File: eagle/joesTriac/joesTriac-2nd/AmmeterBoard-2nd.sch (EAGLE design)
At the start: 37 parts, among them IC2 TLC251P, IC3 TLC251_or_311, IC4 INA118P, IC5 TLC251_or_311, IC6 TLC251P, IC7 ACS758ECB-200B-PFF-T, T1 2N3441, X1 1, X2 2, X6 1751264

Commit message: reg save, working on exti
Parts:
- added X3: 1751264, con-phoenix-350:1751264
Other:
- note added: ". +9"
- note added: ". -9"
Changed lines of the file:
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@@
 <part name="SUPPLY31" library="supply2" deviceset="GND" device=""/>
 <part name="SUPPLY32" library="supply2" deviceset="GND" device=""/>
+<part name="X3" library="con-phoenix-350" deviceset="1751264" device=""/>
 </parts>
 <sheets>
@@
 <text x="139.7" y="58.42" size="1.778" layer="91">eventually aplifier can be ommitted</text>
 <text x="91.44" y="-7.62" size="1.778" layer="91">0V .. 3.3V tobe tested</text>
+<text x="35.56" y="48.26" size="1.778" layer="91">.   -9</text>
+<text x="35.56" y="53.34" size="1.778" layer="91">.   +9</text>
 </plain>
 <instances>
@@
 <instance part="SUPPLY31" gate="GND" x="20.32" y="-12.7"/>
 <instance part="SUPPLY32" gate="GND" x="83.82" y="-20.32"/>
+<instance part="X3" gate="-2" x="22.86" y="53.34"/>
+<instance part="X3" gate="-3" x="22.86" y="48.26"/>
 </instances>
 <busses>
@@
 <pinref part="IC2" gate="A" pin="+IN"/>
 <wire x1="-35.56" y1="2.54" x2="-25.4" y2="2.54" width="0.1524" layer="91"/>
-<wire x1="25.4" y1="76.2" x2="38.1" y2="76.2" width="0.1524" layer="91"/>
-<wire x1="38.1" y1="76.2" x2="38.1" y2="22.86" width="0.1524" layer="91"/>
-<wire x1="38.1" y1="22.86" x2="-35.56" y2="22.86" width="0.1524" layer="91"/>
+<wire x1="43.18" y1="22.86" x2="-35.56" y2="22.86" width="0.1524" layer="91"/>
 <wire x1="-35.56" y1="22.86" x2="-35.56" y2="2.54" width="0.1524" layer="91"/>
-</segment>
-</net>
+<wire x1="43.18" y1="76.2" x2="43.18" y2="22.86" width="0.1524" layer="91"/>
+<wire x1="25.4" y1="76.2" x2="43.18" y2="76.2" width="0.1524" layer="91"/>
+</segment>
+</net>

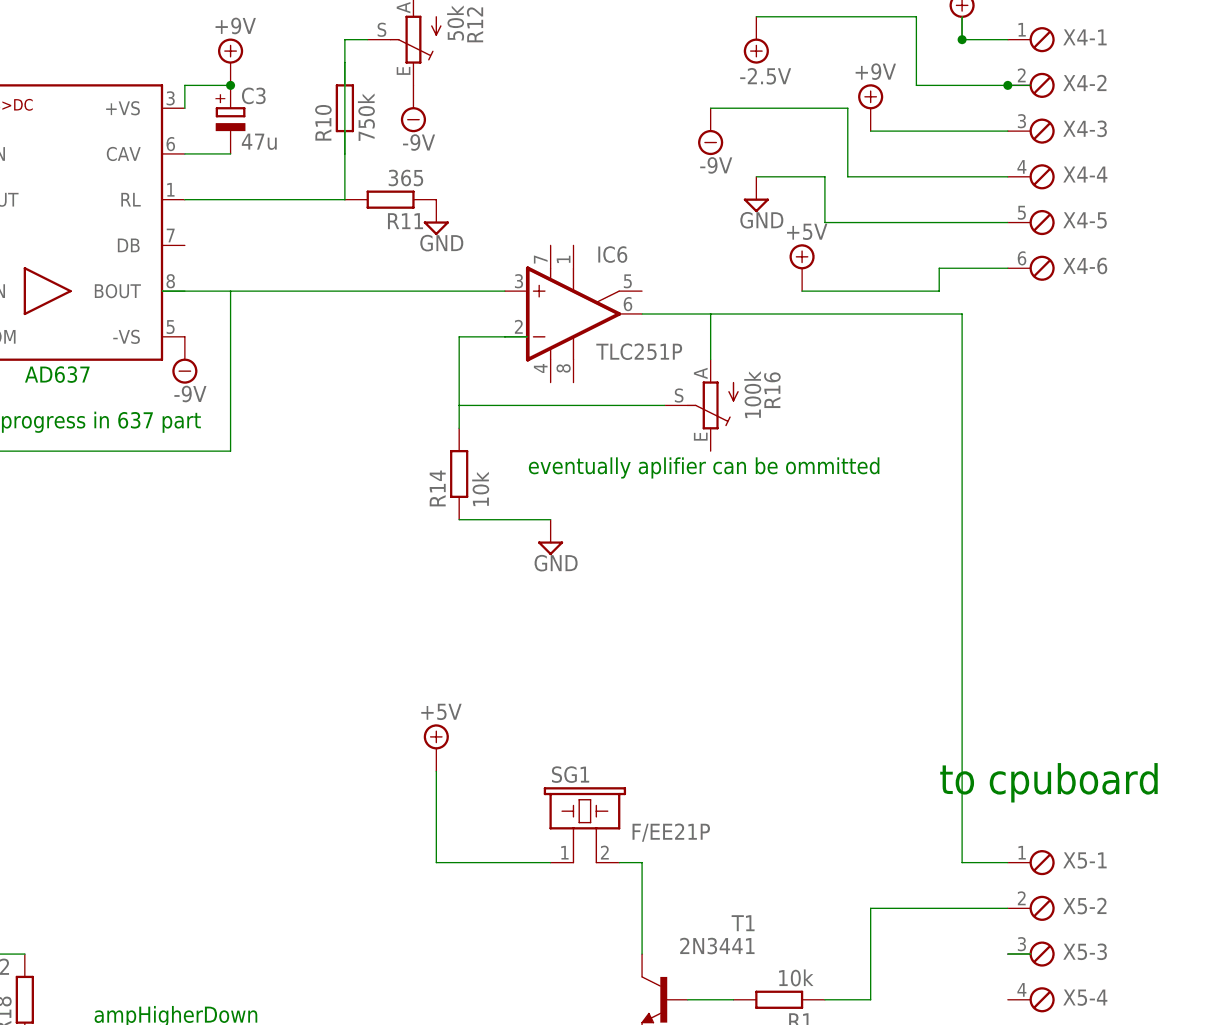
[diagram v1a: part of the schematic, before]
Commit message: reg save, working on exti spikes
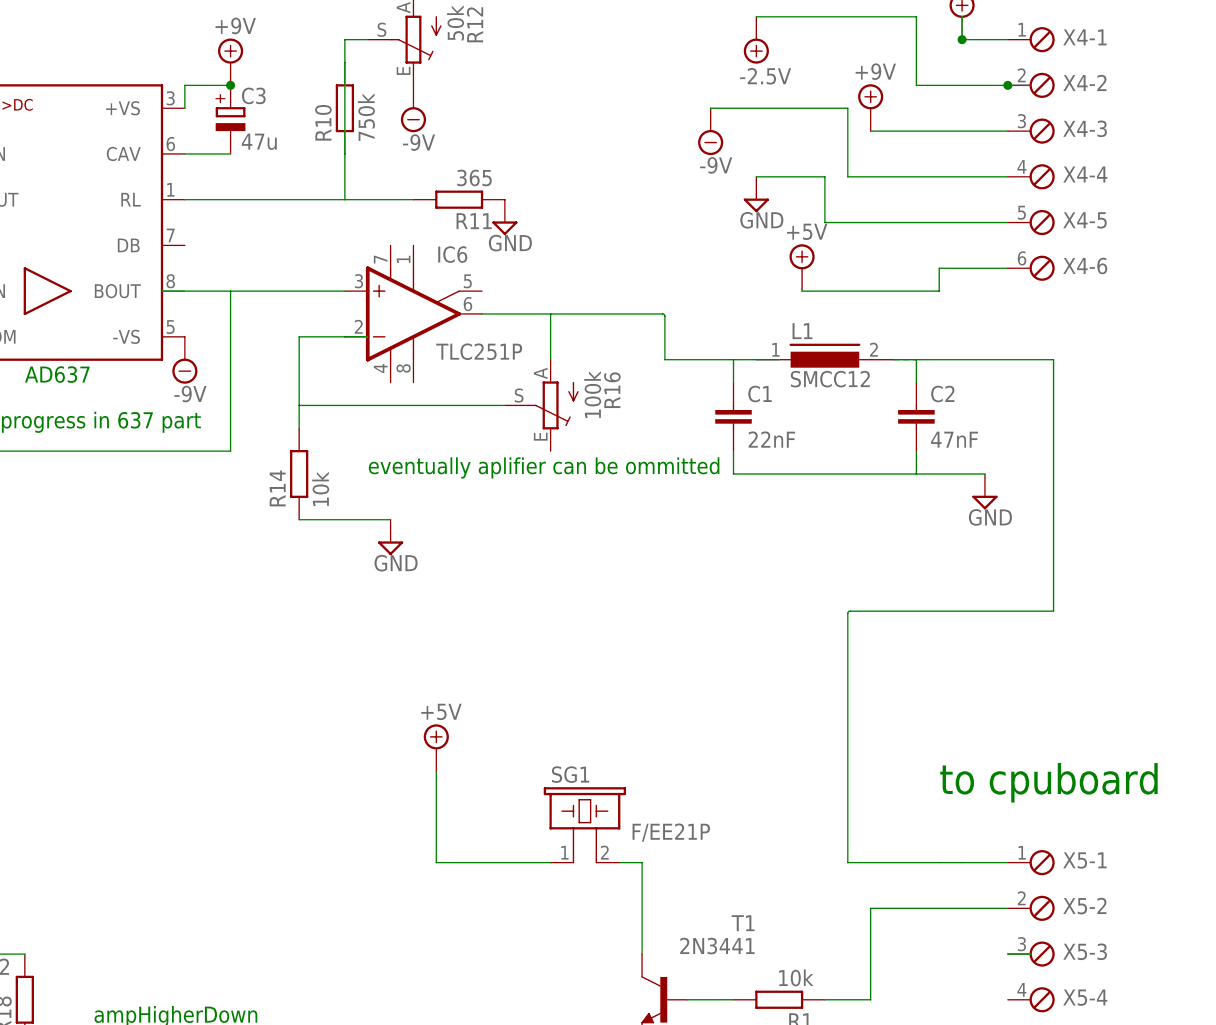
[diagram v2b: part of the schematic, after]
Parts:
- added C1: 22nF, resistor:C-EU050-030X075
- added C2: 47nF, resistor:C-EU050-030X075
- added L1: SMCC12, inductors:SMCC12
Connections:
- removed net N$26 (its old number): IC6.OUT, R16.A, X5-1.1
- new net N$34: C2.1, L1.2, X5-1.1
- new net N$35: C1.1, IC6.OUT, L1.1, R16.A
- net GND: now also C1.2, C2.2
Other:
- moved on the sheet: IC6, R11, R14, R16
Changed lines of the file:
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@@
 <layer number="51" name="tDocu" color="6" fill="1" visible="no" active="no"/>
 <layer number="52" name="bDocu" color="7" fill="1" visible="no" active="no"/>
+<layer number="90" name="Modules" color="5" fill="1" visible="yes" active="yes"/>
 <layer number="91" name="Nets" color="2" fill="1" visible="yes" active="yes"/>
 <layer number="92" name="Busses" color="1" fill="1" visible="yes" active="yes"/>
@@
 <part name="SUPPLY32" library="supply2" deviceset="GND" device=""/>
 <part name="X3" library="con-phoenix-350" deviceset="1751264" device=""/>
+<part name="L1" library="inductors" deviceset="SMCC12" device=""/>
+<part name="C2" library="resistor" deviceset="C-EU" device="050-030X075" value="47nF"/>
+<part name="C1" library="resistor" deviceset="C-EU" device="050-030X075" value="22nF"/>
+<part name="SUPPLY33" library="supply2" deviceset="GND" device=""/>
 </parts>
 <sheets>
@@
 <text x="91.44" y="-2.54" size="1.778" layer="91">ampHigherDown</text>
 <text x="60.96" y="-30.48" size="1.778" layer="91">ampLowerDown / if ok, divider as above</text>
-<text x="139.7" y="58.42" size="1.778" layer="91">eventually aplifier can be ommitted</text>
+<text x="121.92" y="58.42" size="1.778" layer="91">eventually aplifier can be ommitted</text>
 <text x="91.44" y="-7.62" size="1.778" layer="91">0V .. 3.3V tobe tested</text>
 <text x="35.56" y="48.26" size="1.778" layer="91">.   -9</text>
@@
 <instance part="R9" gate="1" x="53.34" y="101.6" rot="R180"/>
 <instance part="R10" gate="G$1" x="119.38" y="99.06" rot="R90"/>
-<instance part="R11" gate="G$1" x="124.46" y="88.9" rot="R180"/>
+<instance part="R11" gate="G$1" x="132.08" y="88.9" rot="R180"/>
 <instance part="R12" gate="1" x="127" y="106.68" rot="R180"/>
 <instance part="SUPPLY7" gate="GND" x="73.66" y="71.12"/>
 <instance part="SUPPLY10" gate="G$1" x="127" y="114.3"/>
 <instance part="SUPPLY11" gate="G$1" x="127" y="99.06"/>
-<instance part="SUPPLY12" gate="GND" x="129.54" y="86.36"/>
+<instance part="SUPPLY12" gate="GND" x="137.16" y="86.36"/>
 <instance part="C3" gate="G$1" x="106.68" y="99.06"/>
 <instance part="SUPPLY13" gate="G$1" x="106.68" y="104.14"/>
@@
 <instance part="R13" gate="G$1" x="66.04" y="83.82" rot="R270"/>
 <instance part="SUPPLY15" gate="GND" x="60.96" y="68.58"/>
-<instance part="IC6" gate="A" x="144.78" y="76.2"/>
-<instance part="R14" gate="G$1" x="132.08" y="58.42" rot="R90"/>
-<instance part="R16" gate="1" x="160.02" y="66.04" rot="R180"/>
-<instance part="SUPPLY16" gate="GND" x="142.24" y="50.8"/>
+<instance part="IC6" gate="A" x="127" y="76.2"/>
+<instance part="R14" gate="G$1" x="114.3" y="58.42" rot="R90"/>
+<instance part="R16" gate="1" x="142.24" y="66.04" rot="R180"/>
+<instance part="SUPPLY16" gate="GND" x="124.46" y="50.8"/>
 <instance part="X4" gate="-1" x="195.58" y="106.68"/>
 <instance part="X4" gate="-2" x="195.58" y="101.6"/>
@@
 <instance part="X3" gate="-2" x="22.86" y="53.34"/>
 <instance part="X3" gate="-3" x="22.86" y="48.26"/>
+<instance part="L1" gate="1" x="172.72" y="71.12"/>
+<instance part="C2" gate="G$1" x="182.88" y="66.04"/>
+<instance part="C1" gate="G$1" x="162.56" y="66.04"/>
+<instance part="SUPPLY33" gate="GND" x="190.5" y="55.88"/>
 </instances>
 <busses>
@@
 </segment>
 <segment>
-<wire x1="132.08" y1="53.34" x2="142.24" y2="53.34" width="0.1524" layer="91"/>
+<wire x1="114.3" y1="53.34" x2="124.46" y2="53.34" width="0.1524" layer="91"/>
 <pinref part="R14" gate="G$1" pin="1"/>
 <pinref part="SUPPLY16" gate="GND" pin="GND"/>
@@
 <pinref part="SUPPLY32" gate="GND" pin="GND"/>
 </segment>
+<segment>
+<pinref part="SUPPLY33" gate="GND" pin="GND"/>
+<wire x1="190.5" y1="58.42" x2="182.88" y2="58.42" width="0.1524" layer="91"/>
+<pinref part="C1" gate="G$1" pin="2"/>
+<wire x1="182.88" y1="58.42" x2="162.56" y2="58.42" width="0.1524" layer="91"/>
+<wire x1="162.56" y1="58.42" x2="162.56" y2="60.96" width="0.1524" layer="91"/>
+<pinref part="C2" gate="G$1" pin="2"/>
+<wire x1="182.88" y1="58.42" x2="182.88" y2="60.96" width="0.1524" layer="91"/>
+</segment>
 </net>
 <net name="N$8" class="0">
@@
 </segment>
 </net>
-<net name="N$19" class="0">
-<segment>
-<wire x1="121.92" y1="106.68" x2="119.38" y2="106.68" width="0.1524" layer="91"/>
-<wire x1="119.38" y1="106.68" x2="119.38" y2="104.14" width="0.1524" layer="91"/>
-<wire x1="119.38" y1="104.14" x2="119.38" y2="93.98" width="0.1524" layer="91"/>
-<wire x1="119.38" y1="93.98" x2="119.38" y2="88.9" width="0.1524" layer="91"/>
-<wire x1="101.6" y1="88.9" x2="119.38" y2="88.9" width="0.1524" layer="91"/>
-<pinref part="R12" gate="1" pin="S"/>
-<pinref part="R10" gate="G$1" pin="2"/>
-<pinref part="R10" gate="G$1" pin="1"/>
-<pinref part="R11" gate="G$1" pin="2"/>
-<pinref part="IC1" gate="G$1" pin="RL"/>
-</segment>
-</net>
 <net name="N$21" class="0">
 <segment>
@@
 <net name="N$25" class="0">
 <segment>
-<wire x1="99.06" y1="78.74" x2="137.16" y2="78.74" width="0.1524" layer="91"/>
+<wire x1="99.06" y1="78.74" x2="119.38" y2="78.74" width="0.1524" layer="91"/>
 <pinref part="IC6" gate="A" pin="+IN"/>
 </segment>
 </net>
-<net name="N$26" class="0">
-<segment>
-<wire x1="152.4" y1="76.2" x2="160.02" y2="76.2" width="0.1524" layer="91"/>
-<wire x1="160.02" y1="76.2" x2="187.96" y2="76.2" width="0.1524" layer="91"/>
-<wire x1="160.02" y1="76.2" x2="160.02" y2="71.12" width="0.1524" layer="91"/>
-<wire x1="187.96" y1="76.2" x2="187.96" y2="15.24" width="0.1524" layer="91"/>
-<pinref part="IC6" gate="A" pin="OUT"/>
-<pinref part="R16" gate="1" pin="A"/>
-<pinref part="X5" gate="-1" pin="1"/>
-<wire x1="187.96" y1="15.24" x2="193.04" y2="15.24" width="0.1524" layer="91"/>
-</segment>
-</net>
 <net name="N$27" class="0">
 <segment>
-<wire x1="132.08" y1="63.5" x2="132.08" y2="66.04" width="0.1524" layer="91"/>
-<wire x1="132.08" y1="66.04" x2="132.08" y2="73.66" width="0.1524" layer="91"/>
-<wire x1="132.08" y1="73.66" x2="137.16" y2="73.66" width="0.1524" layer="91"/>
-<wire x1="139.7" y1="73.66" x2="137.16" y2="73.66" width="0.1524" layer="91"/>
-<wire x1="154.94" y1="66.04" x2="132.08" y2="66.04" width="0.1524" layer="91"/>
+<wire x1="114.3" y1="63.5" x2="114.3" y2="66.04" width="0.1524" layer="91"/>
+<wire x1="114.3" y1="66.04" x2="114.3" y2="73.66" width="0.1524" layer="91"/>
+<wire x1="114.3" y1="73.66" x2="119.38" y2="73.66" width="0.1524" layer="91"/>
+<wire x1="121.92" y1="73.66" x2="119.38" y2="73.66" width="0.1524" layer="91"/>
+<wire x1="137.16" y1="66.04" x2="114.3" y2="66.04" width="0.1524" layer="91"/>
 <pinref part="R14" gate="G$1" pin="2"/>
 <pinref part="IC6" gate="A" pin="-IN"/>
@@
 </segment>
 </net>
+<net name="N$34" class="0">
+<segment>
+<pinref part="L1" gate="1" pin="2"/>
+<wire x1="180.34" y1="71.12" x2="182.88" y2="71.12" width="0.1524" layer="91" style="shortdash"/>
+<wire x1="180.34" y1="71.12" x2="182.88" y2="71.12" width="0.1524" layer="91"/>
+<pinref part="C2" gate="G$1" pin="1"/>
+<wire x1="182.88" y1="71.12" x2="182.88" y2="68.58" width="0.1524" layer="91"/>
+<wire x1="182.88" y1="71.12" x2="198.12" y2="71.12" width="0.1524" layer="91"/>
+<wire x1="198.12" y1="71.12" x2="198.12" y2="43.18" width="0.1524" layer="91"/>
+<wire x1="198.12" y1="43.18" x2="175.514" y2="43.18" width="0.1524" layer="91"/>
+<wire x1="175.514" y1="43.18" x2="175.26" y2="42.926" width="0.1524" layer="91" curve="90"/>
+<wire x1="175.26" y1="42.926" x2="175.26" y2="15.24" width="0.1524" layer="91"/>
+<pinref part="X5" gate="-1" pin="1"/>
+<wire x1="175.26" y1="15.24" x2="185.42" y2="15.24" width="0.1524" layer="91"/>
+<wire x1="187.96" y1="15.24" x2="193.04" y2="15.24" width="0.1524" layer="91"/>
+<wire x1="187.96" y1="15.24" x2="185.42" y2="15.24" width="0.1524" layer="91"/>
+</segment>
+</net>
+<net name="N$35" class="0">
+<segment>
+<pinref part="R16" gate="1" pin="A"/>
+<wire x1="142.24" y1="76.2" x2="142.24" y2="71.12" width="0.1524" layer="91"/>
+<wire x1="134.62" y1="76.2" x2="142.24" y2="76.2" width="0.1524" layer="91"/>
+<pinref part="IC6" gate="A" pin="OUT"/>
+<wire x1="154.94" y1="71.12" x2="162.56" y2="71.12" width="0.1524" layer="91"/>
+<pinref part="C1" gate="G$1" pin="1"/>
+<wire x1="162.56" y1="71.12" x2="165.1" y2="71.12" width="0.1524" layer="91"/>
+<wire x1="165.1" y1="71.12" x2="167.64" y2="71.12" width="0.1524" layer="91"/>
+<wire x1="162.56" y1="71.12" x2="162.56" y2="68.58" width="0.1524" layer="91"/>
+<pinref part="L1" gate="1" pin="1"/>
+<wire x1="142.24" y1="76.2" x2="154.686" y2="76.2" width="0.1524" layer="91"/>
+<wire x1="154.686" y1="76.2" x2="154.94" y2="75.946" width="0.1524" layer="91" curve="-90"/>
+<wire x1="154.94" y1="75.946" x2="154.94" y2="71.12" width="0.1524" layer="91"/>
+</segment>
+</net>
+<net name="N$26" class="0">
+<segment>
+<pinref part="R12" gate="1" pin="S"/>
+<wire x1="121.92" y1="106.68" x2="119.38" y2="106.68" width="0.1524" layer="91"/>
+<wire x1="119.38" y1="106.68" x2="119.38" y2="104.14" width="0.1524" layer="91"/>
+<pinref part="R10" gate="G$1" pin="2"/>
+<wire x1="119.38" y1="104.14" x2="119.38" y2="93.98" width="0.1524" layer="91"/>
+<pinref part="R10" gate="G$1" pin="1"/>
+<wire x1="101.6" y1="88.9" x2="119.38" y2="88.9" width="0.1524" layer="91"/>
+<pinref part="R11" gate="G$1" pin="2"/>
+<pinref part="IC1" gate="G$1" pin="RL"/>
+<wire x1="119.38" y1="88.9" x2="127" y2="88.9" width="0.1524" layer="91"/>
+<wire x1="119.38" y1="93.98" x2="119.38" y2="88.9" width="0.1524" layer="91"/>
+</segment>
+</net>
